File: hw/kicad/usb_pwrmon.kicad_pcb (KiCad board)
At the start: 2 copper layers, 45.2 x 21.8 mm, 31 parts, among them J1 ARM_10PIN, J2 USB_MALE_A, J3 USB_FEMALE_A, P1 TST, P2 TST, P3 TST, P4 TST, SW1 SW_PUSH, U1 AD8293G80, U2 MKL02ZXVFG4, U3 AAT3221

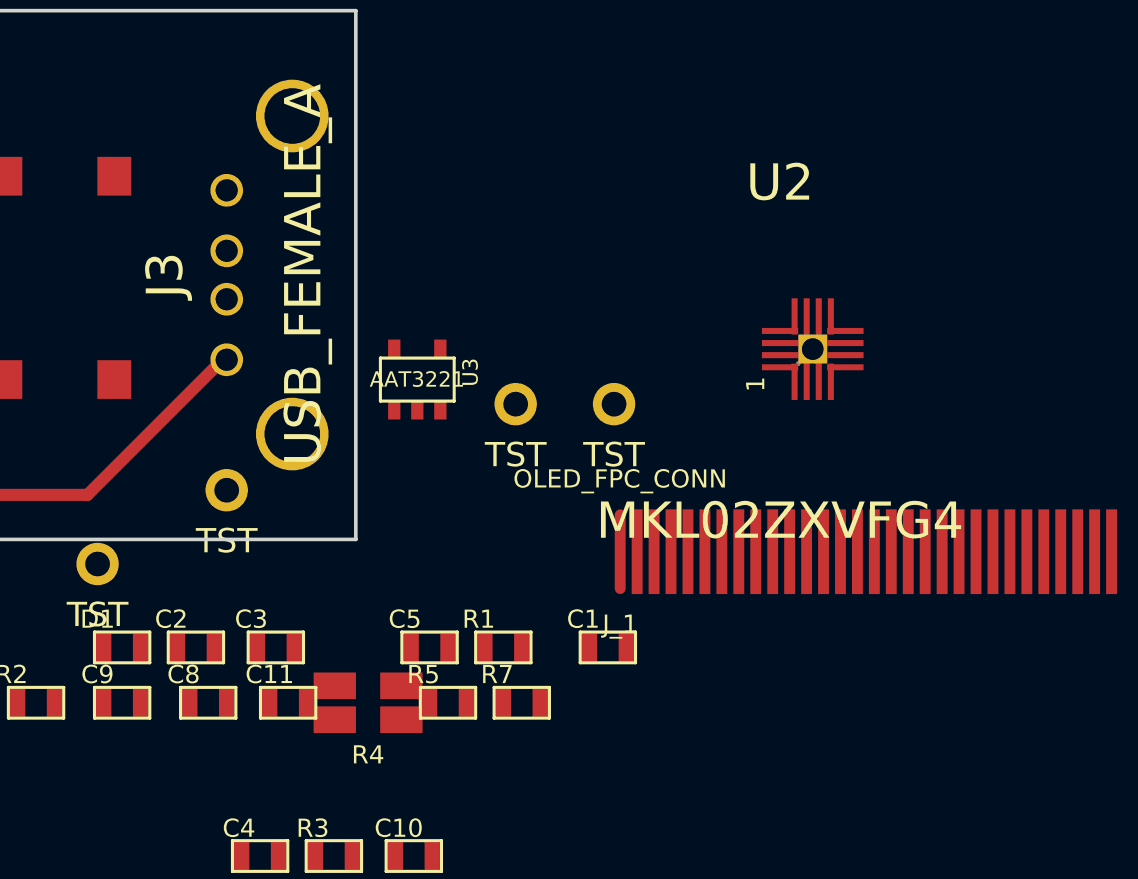
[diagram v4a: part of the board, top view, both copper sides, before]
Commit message: - replace footprints on pcb
Former-commit-id: 5cc941f39f571a50f1e83a40c3593a89abae6803
Former-commit-id: affb5e9e8c4de2429eb32b667997dfb1650dbaf3
Former-commit-id: c77c17cd257b42edf55da28a0b3895ffc35f362b
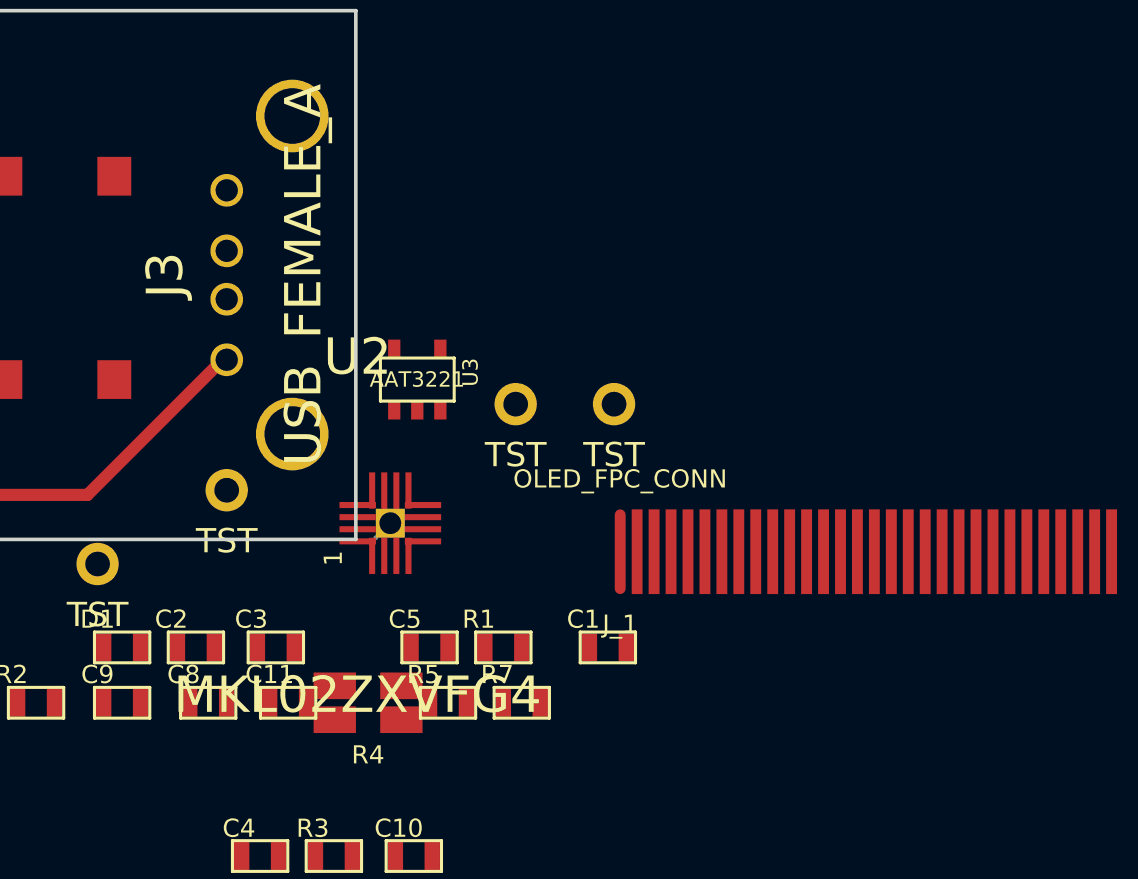
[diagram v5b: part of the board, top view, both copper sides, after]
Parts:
- moved U2 18.9 mm to (117.4, 43.0)
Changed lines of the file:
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@@
+    )
+  )
+  (module ARM_10_PIN_SMT (layer F.Cu)
+    (at 95.25 27.178)
+    (fp_text reference J1 (at 0 -4) (layer F.SilkS)
+      (effects (font (size 1 1) (thickness 0.15)))
+    )
+    (fp_text value ARM_10PIN (at 0 4) (layer F.SilkS)
+      (effects (font (size 1 1) (thickness 0.15)))
+    )
+    (pad 1 smd oval (at -2.5 2.175) (size 0.76 1.75)
+      (layers F.Cu F.Paste F.Mask)
+      (net 2 +3.3v)
+    )
+    (pad 2 smd rect (at -2.5 -2.175) (size 0.76 1.75)
+      (layers F.Cu F.Paste F.Mask)
+      (net 23 SWDIO)
+    )
+    (pad 3 smd rect (at -1.23 2.175) (size 0.76 1.75)
+      (layers F.Cu F.Paste F.Mask)
+      (net 4 GND)
+    )
+    (pad 4 smd rect (at -1.23 -2.175) (size 0.76 1.75)
+      (layers F.Cu F.Paste F.Mask)
+      (net 22 SWCLK)
+    )
+    (pad 5 smd rect (at 0.04 2.175) (size 0.76 1.75)
+      (layers F.Cu F.Paste F.Mask)
+      (net 4 GND)
+    )
+    (pad 6 smd rect (at 0.04 -2.175) (size 0.76 1.75)
+      (layers F.Cu F.Paste F.Mask)
+    )
+    (pad 7 smd rect (at 1.31 2.175) (size 0.76 1.75)
+      (layers F.Cu F.Paste F.Mask)
+    )
+    (pad 8 smd rect (at 1.31 -2.175) (size 0.76 1.75)
+      (layers F.Cu F.Paste F.Mask)
+    )
+    (pad 9 smd rect (at 2.58 2.175) (size 0.76 1.75)
+      (layers F.Cu F.Paste F.Mask)
+      (net 4 GND)
+    )
+    (pad 10 smd rect (at 2.58 -2.175) (size 0.76 1.75)
+      (layers F.Cu F.Paste F.Mask)
+      (net 19 NRESET)
     )
   )
   (module MKL02_QFN16 (layer F.Cu)
-    (at 134.874 35.814)
+    (at 117.423001 43.006001)
     (fp_text reference U2 (at 0 -7.62) (layer F.SilkS)
       (effects (font (size 1.5 1.5) (thickness 0.15)))
@@
     )
   )
-  (module ARM_10_PIN_SMT (layer F.Cu)
-    (at 95.25 27.178)
-    (fp_text reference J1 (at 0 -4) (layer F.SilkS)
-      (effects (font (size 1 1) (thickness 0.15)))
-    )
-    (fp_text value ARM_10PIN (at 0 4) (layer F.SilkS)
-      (effects (font (size 1 1) (thickness 0.15)))
-    )
-    (pad 1 smd oval (at -2.5 2.175) (size 0.76 1.75)
-      (layers F.Cu F.Paste F.Mask)
-      (net 2 +3.3v)
-    )
-    (pad 2 smd rect (at -2.5 -2.175) (size 0.76 1.75)
-      (layers F.Cu F.Paste F.Mask)
-      (net 23 SWDIO)
-    )
-    (pad 3 smd rect (at -1.23 2.175) (size 0.76 1.75)
-      (layers F.Cu F.Paste F.Mask)
-      (net 4 GND)
-    )
-    (pad 4 smd rect (at -1.23 -2.175) (size 0.76 1.75)
-      (layers F.Cu F.Paste F.Mask)
-      (net 22 SWCLK)
-    )
-    (pad 5 smd rect (at 0.04 2.175) (size 0.76 1.75)
-      (layers F.Cu F.Paste F.Mask)
-      (net 4 GND)
-    )
-    (pad 6 smd rect (at 0.04 -2.175) (size 0.76 1.75)
-      (layers F.Cu F.Paste F.Mask)
-    )
-    (pad 7 smd rect (at 1.31 2.175) (size 0.76 1.75)
-      (layers F.Cu F.Paste F.Mask)
-    )
-    (pad 8 smd rect (at 1.31 -2.175) (size 0.76 1.75)
-      (layers F.Cu F.Paste F.Mask)
-    )
-    (pad 9 smd rect (at 2.58 2.175) (size 0.76 1.75)
-      (layers F.Cu F.Paste F.Mask)
-      (net 4 GND)
-    )
-    (pad 10 smd rect (at 2.58 -2.175) (size 0.76 1.75)
-      (layers F.Cu F.Paste F.Mask)
-      (net 19 NRESET)
-    )
-  )

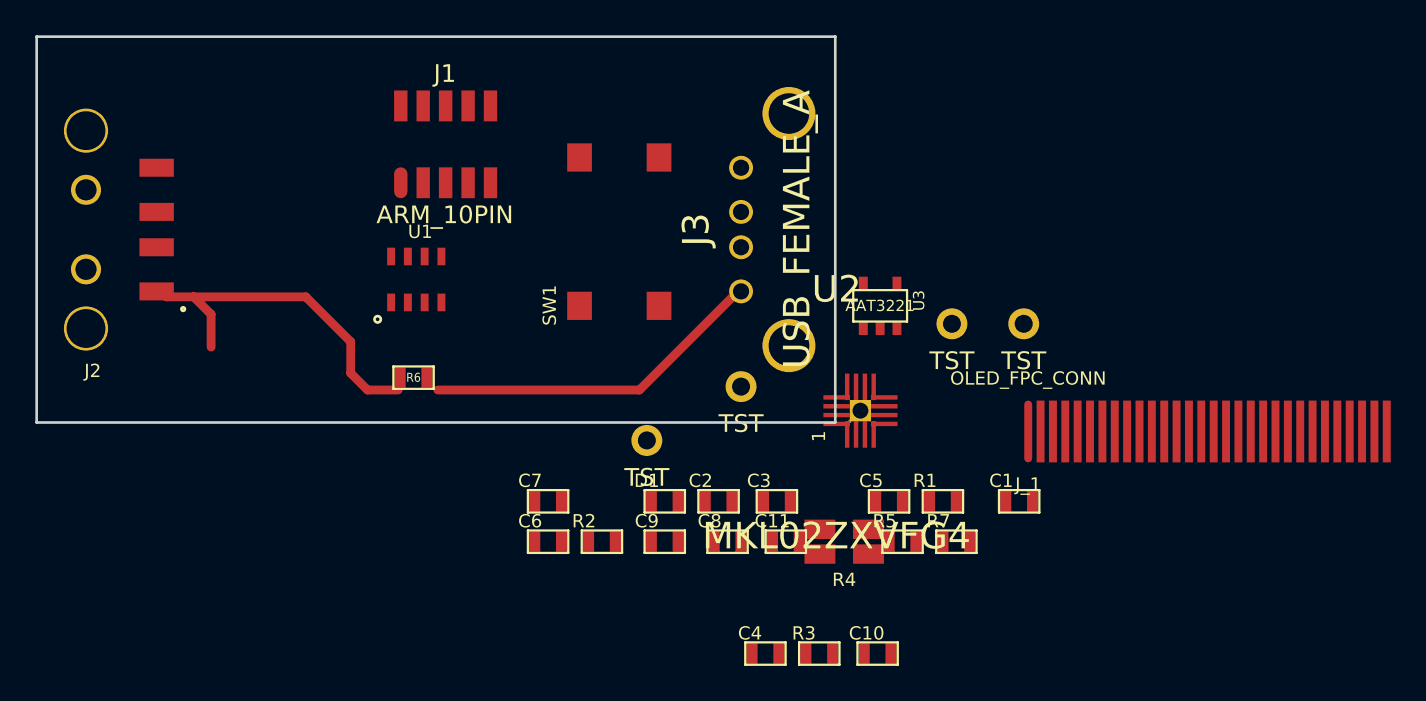
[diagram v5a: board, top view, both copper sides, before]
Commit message: - layout about 1/2 done
Former-commit-id: d0cff35ed20b8f19404ca1928e0e4c997e9cc0fb
Former-commit-id: 4a8e0d8b3233680ff7140ac2bf066568b7e4d971
Former-commit-id: 2e3a7731e31c3aed773827895a43c1fdf13a017a
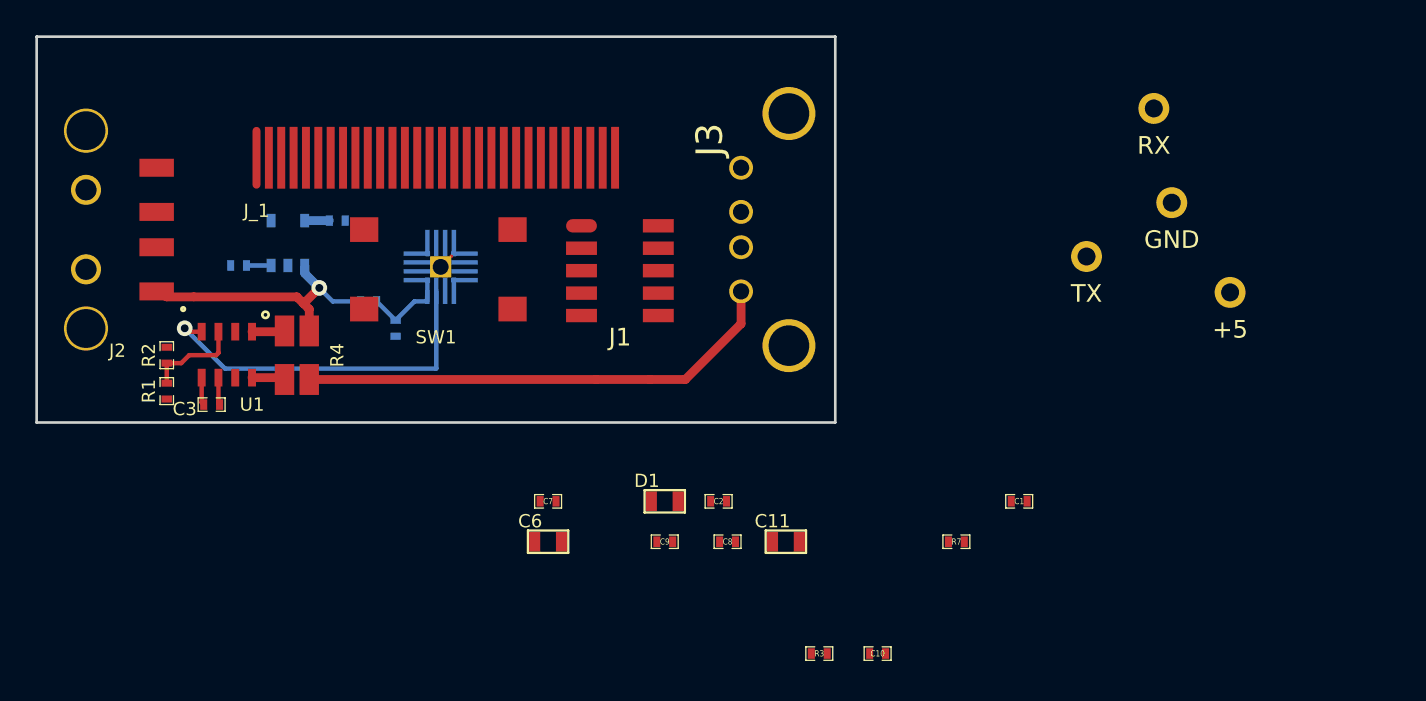
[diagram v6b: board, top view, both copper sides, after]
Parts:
- C1, C10, C2, C3, C7, C8, C9, R1, R2, R3, R7: footprint SM0603 -> SM0402
- C4, C5, R5, R6: footprint SM0603 -> SM0402; moved to B.Cu
- P1: value TST -> TX
- P2: value TST -> RX
- P3: value TST -> GND
- P4: value TST -> +5
- U2, U3: moved to B.Cu
- moved J_1 46.4 mm to (84.6, 27.9)
- moved R1 44.4 mm to (79.5, 41.1), turned to 270 degrees
- moved C4 37.0 mm to (83.6, 34.0), turned to 180 degrees
- moved C5 35.0 mm to (89.2, 31.5)
- moved P2 34.3 mm to (135.4, 25.1)
- moved U3 33.7 mm to (86.4, 32.8), turned to 180 degrees
- moved R5 33.1 mm to (90.9, 36.1)
- moved R4 32.7 mm to (86.9, 39.1), turned to 270 degrees
- moved C3 32.5 mm to (82.0, 41.9), turned to 180 degrees
- moved R2 26.8 mm to (79.5, 39.1), turned to 90 degrees
- moved U2 24.0 mm to (95.8, 32.8), turned to 270 degrees
- moved P1 20.9 mm to (131.6, 33.5)
- moved P3 14.2 mm to (136.4, 30.5)
- moved SW1 12.9 mm to (90.7, 32.0), turned to 0 degrees
- moved J1 12.2 mm to (105.2, 34.3), turned to 270 degrees
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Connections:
- net N-0000011 renamed SW_SNS
- J_1 pad 13: (no net) -> OLED_~CS
- J_1 pad 14: (no net) -> OLED_~RST
- J_1 pad 15: (no net) -> OLED_DC/I2X_SA0
- J_1 pad 18: (no net) -> OLED_D0/SPI_SCLK/I2C_SCK
- J_1 pad 19: (no net) -> OLED_D1/SPI_SDIN/I2C_SDA
- U2 pad 13: (no net) -> OLED_~RST
- U2 pad 5: (no net) -> OLED_~CS
- U2 pad 6: (no net) -> OLED_DC/I2X_SA0
- U2 pad 7: (no net) -> OLED_D1/SPI_SDIN/I2C_SDA
- U2 pad 8: (no net) -> OLED_D0/SPI_SCLK/I2C_SCK
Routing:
- net ADC_OUT: track 0.00 -> 20.6 mm, vias 0 -> 1
- net N-0000026: track 19.3 -> 29.5 mm
- net N-0000013: track 0.00 -> 5.50 mm
- net VBUS_SENSE: track 0.00 -> 4.34 mm
- net N-0000015: track 0.00 -> 1.57 mm
- net N-0000014: track 0.00 -> 1.55 mm
- net +3.3: track 0.00 -> 1.39 mm
- net USB_VBUS: track 20.2 -> 19.0 mm, vias 0 -> 1

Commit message: - layout, fin.
Former-commit-id: 1444a8c4e3a8a7bb04b26d5656e94707f8be61c6
Former-commit-id: 8131be0fe2e36c50882f0abde1f1b9a889348b55
Former-commit-id: 0cd6e0f0a4e3ab828657019928c1f3fb57310049
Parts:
- removed P4: +5, TEST_0.100
- C10, C11, C6, C7, C8, C9, R7: moved to B.Cu
- moved SW1 166.6 mm to (204.2, 153.9), turned to 180 degrees
- moved C3 157.6 mm to (187.2, 159.3)
- moved J1 157.6 mm to (210.3, 151.6), turned to 90 degrees
- moved J2 157.6 mm to (180.1, 149.4)
- moved J3 157.6 mm to (217.2, 149.4)
- moved J_1 157.6 mm to (189.7, 145.3)
- moved R1 157.6 mm to (184.7, 158.5)
- moved U1 157.6 mm to (189.5, 157.7)
- moved U2 157.6 mm to (200.9, 150.1)
- moved U3 157.6 mm to (191.5, 150.1)
- moved C4 157.6 mm to (188.7, 151.4)
- moved C5 157.6 mm to (194.3, 148.8)
- moved R2 157.6 mm to (184.7, 156.5)
- moved R4 157.6 mm to (192.0, 156.5)
- moved R5 157.6 mm to (196.1, 153.4)
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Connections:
- C10 pad 2: +3.3 -> +3.3v
- C5 pad 1: +3.3 -> +3.3v
- C9 pad 2: +3.3 -> +3.3v
- J_1 pad 6: +3.3 -> +3.3v
- J_1 pad 9: +3.3 -> +3.3v
- U3 pad 5: +3.3 -> +3.3v
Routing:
- net +3.3v: track 0.00 -> 59.4 mm, vias 0 -> 7
- net USB_DP: track 0.00 -> 46.4 mm
- net USB_DM: track 0.00 -> 44.1 mm
- net N-0000012: track 0.00 -> 20.7 mm, vias 0 -> 3
- net OLED_~RST: track 0.00 -> 17.9 mm, vias 0 -> 3
- net OLED_D1/SPI_SDIN/I2C_SDA: track 0.00 -> 13.3 mm, vias 0 -> 3
- net OLED_D0/SPI_SCLK/I2C_SCK: track 0.00 -> 12.2 mm, vias 0 -> 1
- net NRESET: track 0.00 -> 10.1 mm, vias 0 -> 1
- net SWDIO: track 0.00 -> 9.65 mm, vias 0 -> 1
- net OLED_DC/I2X_SA0: track 0.00 -> 9.11 mm, vias 0 -> 1
- net SERIAL_RX: track 0.00 -> 9.06 mm
- net SERIAL_TX: track 0.00 -> 7.47 mm
- net GND: track 0.00 -> 7.45 mm, vias 0 -> 1
- net SWCLK: track 0.00 -> 7.11 mm, vias 0 -> 1
- net SW_SNS: track 0.00 -> 6.94 mm, vias 0 -> 1
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- added copper zone on B.Cu, net GND
- added copper zone on F.Cu, net GND
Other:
- outline, holes or cut-outs redrawn
- board text added: "git.io/_cXLQQ v0.3"
- board text added: "usb pwr mon"

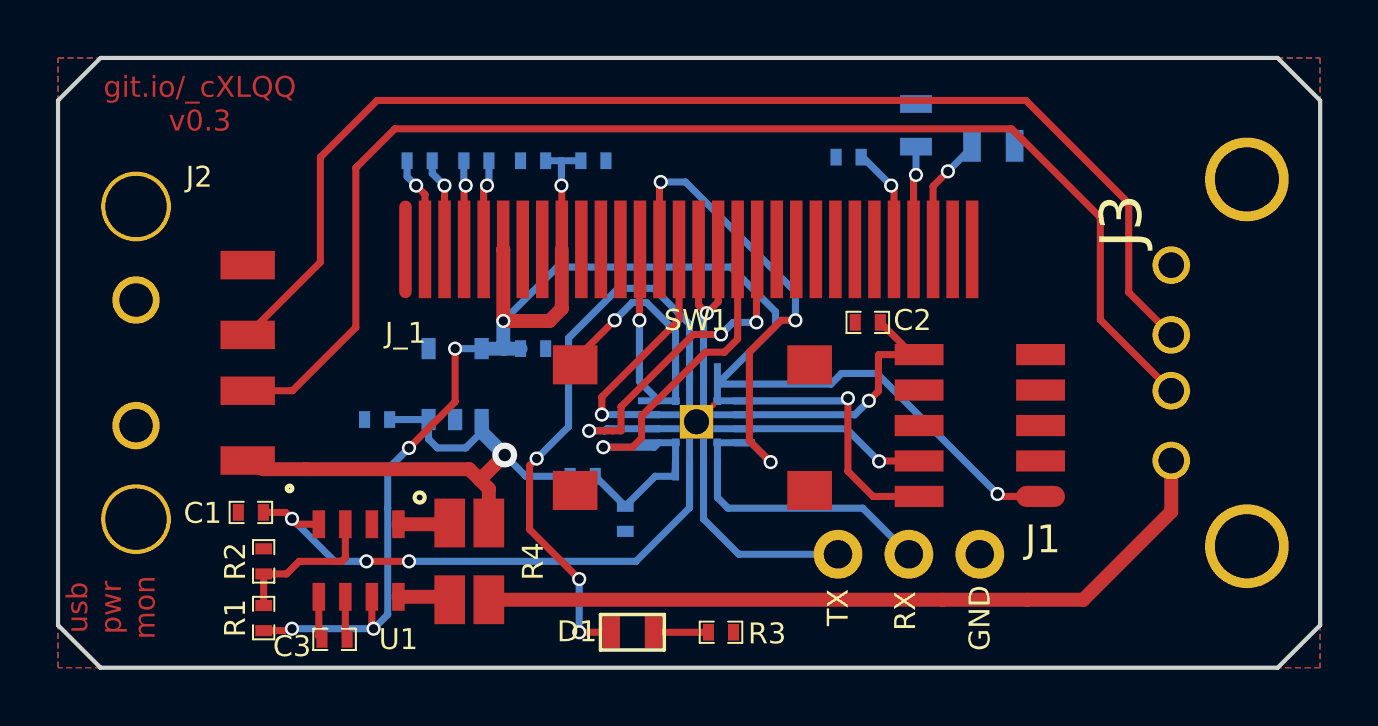
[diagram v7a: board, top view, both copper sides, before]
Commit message: - fix layout with corrected footprint for micro
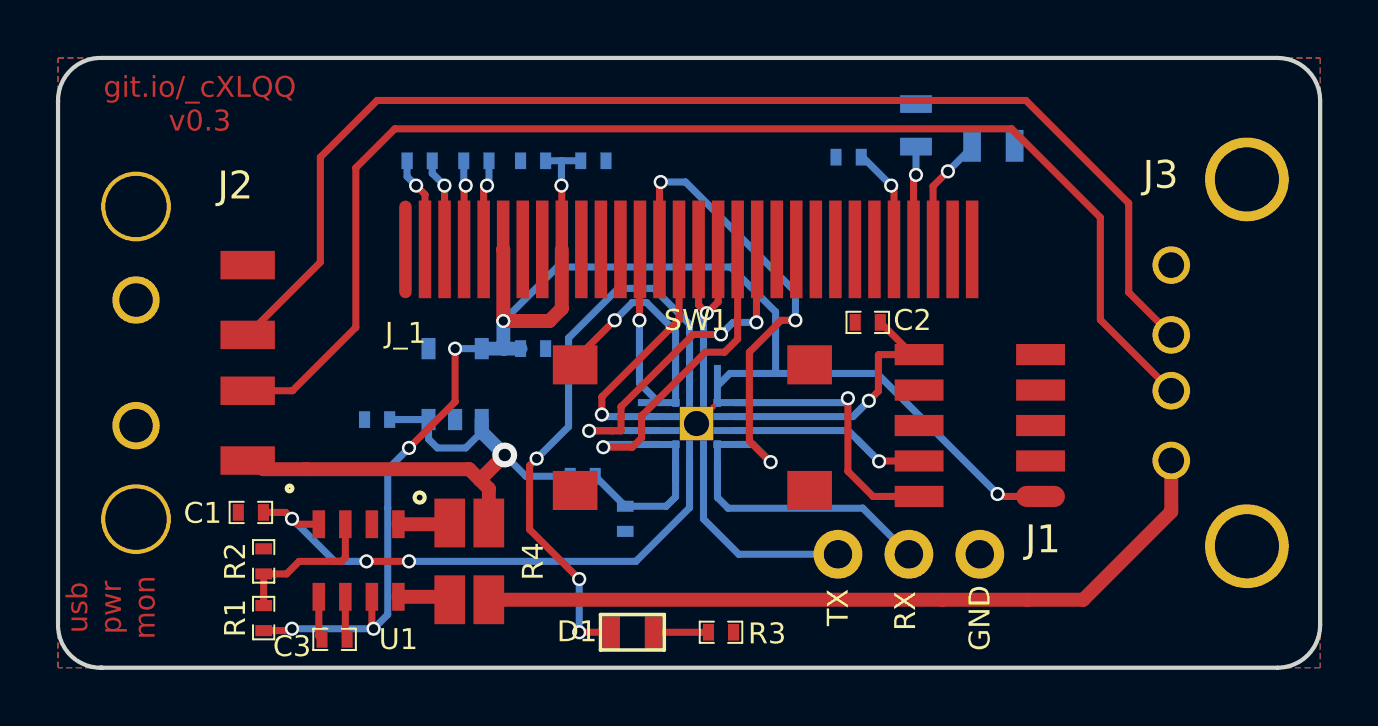
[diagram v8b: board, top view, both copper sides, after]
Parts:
- moved U2 0.06 mm to (200.9, 150.2)
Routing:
- net +3.3v: track 59.4 -> 58.1 mm
- net SWCLK: track 7.11 -> 8.18 mm
- net NRESET: track 10.1 -> 10.9 mm
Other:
- outline, holes or cut-outs redrawn
